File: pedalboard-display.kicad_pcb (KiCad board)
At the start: 2 copper layers, 174 x 111 mm, 206 parts, among them J1 LED-IN, J2 LED-OUT, J3 OLED

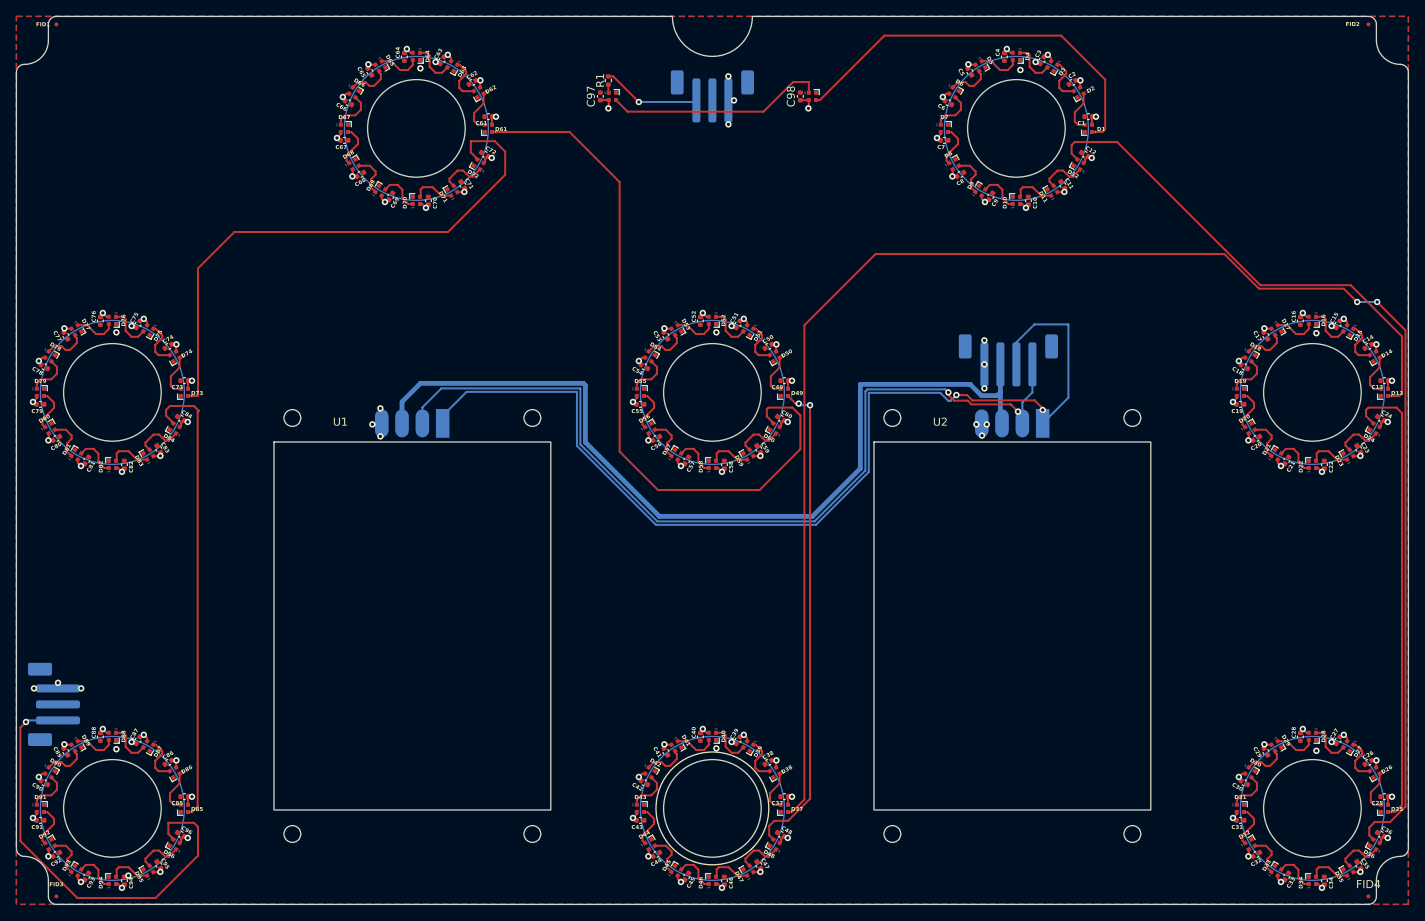
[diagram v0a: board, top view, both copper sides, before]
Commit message: Fix Silkscreen warnings
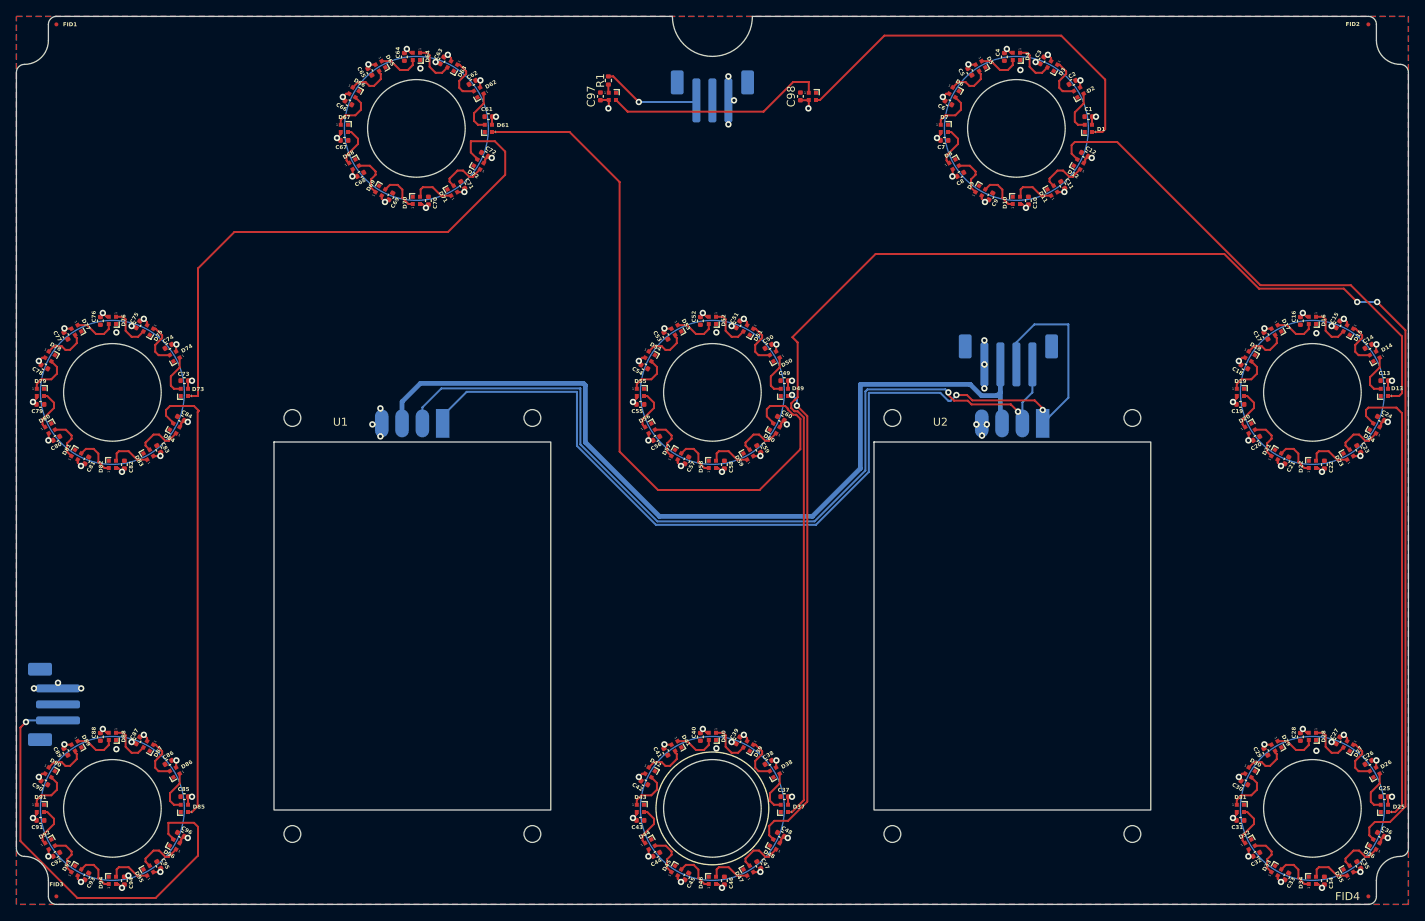
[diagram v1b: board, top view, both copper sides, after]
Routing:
- net /Led Ring B/D_IN: track 211.6 -> 213.7 mm
- net /Led Ring B/D_OUT: track 60.9 -> 60.1 mm

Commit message: Cleanup tracks (move vias to save space
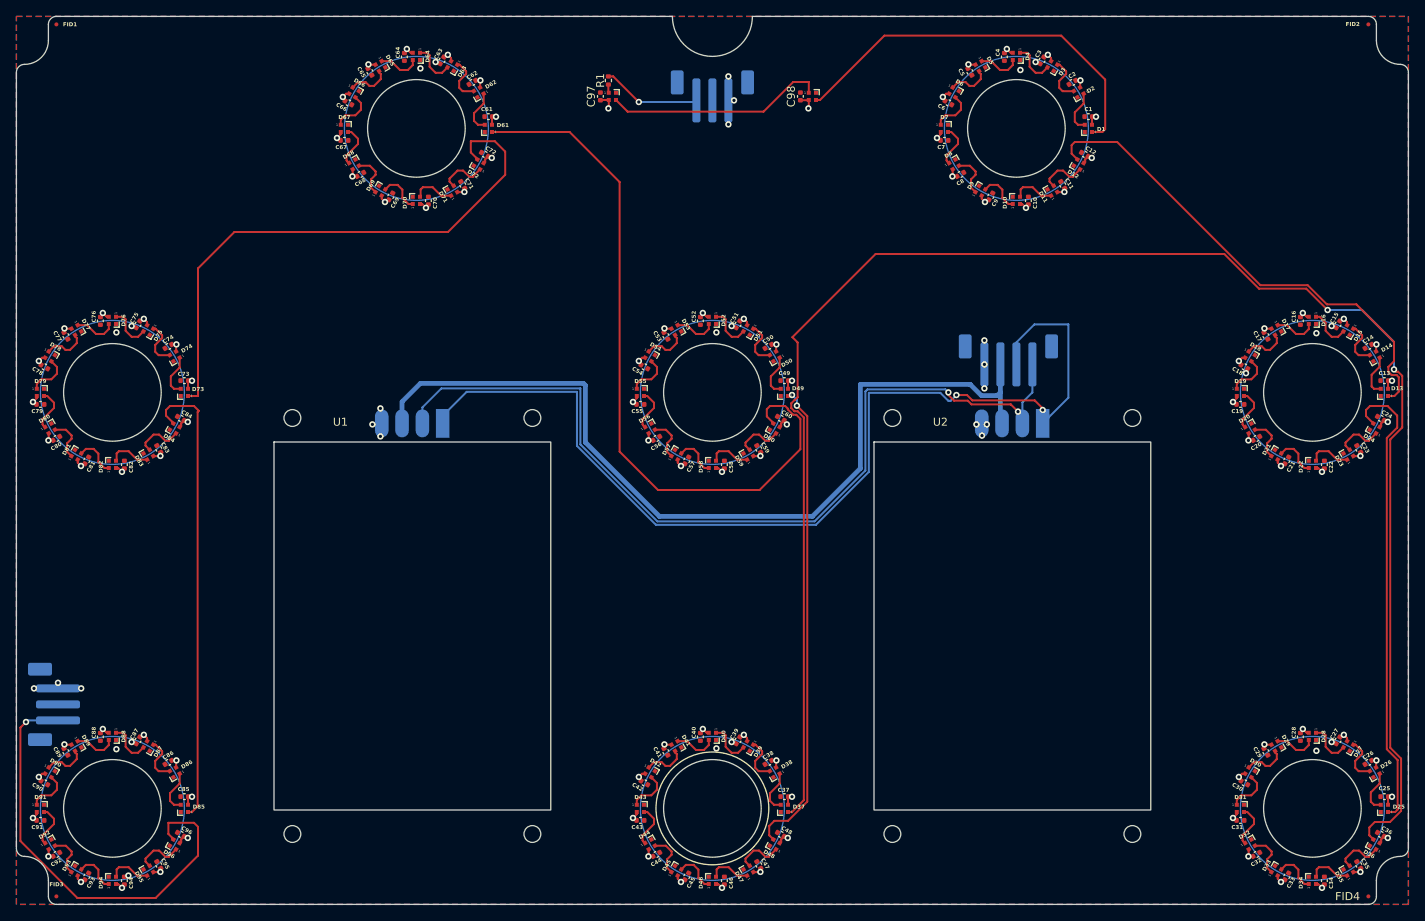
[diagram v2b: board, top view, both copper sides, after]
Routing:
- net GND: track 26.7 -> 25.2 mm, vias 32 -> 33
- net /I2C_SDA: track 127.8 -> 126.9 mm
- net /Led Ring B/D_IN: track 213.7 -> 212.9 mm
- net /Led Ring F/D_IN: track 62.6 -> 61.9 mm

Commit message: Cleanup tracks
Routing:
- net /I2C_SDA: track 126.9 -> 124.9 mm
- net +3.3V: track 110.4 -> 108.8 mm

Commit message: Cleanup vias
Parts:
- moved R1 0.77 mm to (93.4, 33.5), turned to 0 degrees
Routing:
- net GND: track 25.2 -> 20.4 mm
- net Net-(J1-Pin_3): track 12.1 -> 13.4 mm
- net VCC: track 98.9 -> 97.8 mm
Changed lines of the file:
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@@
 	(footprint "Resistor_SMD:R_0402_1005Metric"
 		(layer "F.Cu")
-		(at 94 33.01 -90)
+		(at 93.4 33.5)
 		(descr "Resistor SMD 0402 (1005 Metric), square (rectangular) end terminal, IPC_7351 nominal, (Body size source: IPC-SM-782 page 72, https://www.pcb-3d.com/wordpress/wp-content/uploads/ipc-sm-782a_amendment_1_and_2.pdf), generated with kicad-footprint-generator")
 		(tags "resistor")
 		(property "Reference" "R1"
-			(at 0 1 90)
+			(at 0 1 360)
 			(layer "F.SilkS")
 			(effects
@@
 		)
 		(property "Value" "330"
-			(at 0 1.17 90)
+			(at 0 1.17 360)
 			(layer "F.Fab")
 			(effects
@@
 		)
 		(property "Footprint" "Resistor_SMD:R_0402_1005Metric"
-			(at 0 0 90)
+			(at 0 0 360)
 			(layer "F.Fab")
 			(hide yes)
@@
 		)
 		(property "Datasheet" "https://www.passivecomponent.com/wp-content/uploads/chipR/ASC_WR.pdf"
-			(at 0 0 90)
+			(at 0 0 360)
 			(layer "F.Fab")
 			(hide yes)
@@
 		)
 		(property "Description" ""
-			(at 0 0 90)
+			(at 0 0 360)
 			(layer "F.Fab")
 			(hide yes)
@@
 		)
 		(property "Supplier" "https://www.digikey.ch/en/products/detail/walsin-technology-corporation/WR04X3300FTL/13239224"
-			(at 189 67 90)
+			(at 189 67 360)
 			(layer "F.Fab")
 			(hide yes)
@@
 		(attr smd)
 		(fp_line
-			(start -0.153641 0.38)
-			(end 0.153641 0.38)
+			(start -0.153641 -0.38)
+			(end 0.153641 -0.38)
 			(stroke
 				(width 0.12)
@@
 		)
 		(fp_line
-			(start -0.153641 -0.38)
-			(end 0.153641 -0.38)
+			(start -0.153641 0.38)
+			(end 0.153641 0.38)
 			(stroke
 				(width 0.12)
@@
 		)
 		(fp_line
-			(start -0.93 0.47)
-			(end -0.93 -0.47)
+			(start -0.93 -0.47)
+			(end 0.93 -0.47)
 			(stroke
 				(width 0.05)
@@
 		)
 		(fp_line
-			(start 0.93 0.47)
-			(end -0.93 0.47)
+			(start -0.93 0.47)
+			(end -0.93 -0.47)
 			(stroke
 				(width 0.05)
@@
 		)
 		(fp_line
-			(start -0.93 -0.47)
-			(end 0.93 -0.47)
+			(start 0.93 -0.47)
+			(end 0.93 0.47)
 			(stroke
 				(width 0.05)
@@
 		)
 		(fp_line
-			(start 0.93 -0.47)
-			(end 0.93 0.47)
+			(start 0.93 0.47)
+			(end -0.93 0.47)
 			(stroke
 				(width 0.05)
@@
 		)
 		(fp_line
-			(start -0.525 0.27)
-			(end -0.525 -0.27)
+			(start -0.525 -0.27)
+			(end 0.525 -0.27)
 			(stroke
 				(width 0.1)
@@
 		)
 		(fp_line
-			(start 0.525 0.27)
-			(end -0.525 0.27)
+			(start -0.525 0.27)
+			(end -0.525 -0.27)
 			(stroke
 				(width 0.1)
@@
 		)
 		(fp_line
-			(start -0.525 -0.27)
-			(end 0.525 -0.27)
+			(start 0.525 -0.27)
+			(end 0.525 0.27)
 			(stroke
 				(width 0.1)
@@
 		)
 		(fp_line
-			(start 0.525 -0.27)
-			(end 0.525 0.27)
+			(start 0.525 0.27)
+			(end -0.525 0.27)
 			(stroke
 				(width 0.1)
@@
 		)
 		(fp_text user "${REFERENCE}"
-			(at 0 0 90)
+			(at 0 0 360)
 			(layer "F.Fab")
 			(effects
@@
 		)
 		(pad "1" smd roundrect
-			(at -0.51 0 270)
+			(at -0.51 0)
 			(size 0.54 0.64)
 			(layers "F.Cu" "F.Paste" "F.Mask")
@@
 		)
 		(pad "2" smd roundrect
-			(at 0.51 0 270)
+			(at 0.51 0)
 			(size 0.54 0.64)
 			(layers "F.Cu" "F.Paste" "F.Mask")
@@
 	)
 	(segment
-		(start 94.05 36.45)
-		(end 94 36.5)
-		(width 0.25)
-		(layer "F.Cu")
-		(net 7)
-	)
-	(segment
 		(start 172.803848 120.071797)
 		(end 173.210934 119.664711)
@@
 	)
 	(segment
-		(start 94.05 35.45)
-		(end 94.05 36.45)
-		(width 0.25)
-		(layer "F.Cu")
-		(net 7)
-	)
-	(segment
 		(start 176.04106 116.04106)
 		(end 176 116)
@@
 	)
 	(via
-		(at 94 36.5)
+		(at 94.1 36)
 		(size 0.8)
 		(drill 0.4)
@@
 	)
 	(via
-		(at 65.5 77.5)
+		(at 65.6 77.3)
 		(size 0.8)
 		(drill 0.4)
@@
 	)
 	(via
-		(at 109.7 35.5)
+		(at 109 35.5)
 		(size 0.8)
 		(drill 0.4)
@@
 	)
 	(via
-		(at 25.2 108.3)
+		(at 25.2 109)
 		(size 0.8)
 		(drill 0.4)
@@
 	)
 	(via
-		(at 65.5 74)
+		(at 66.3 76)
 		(size 0.8)
 		(drill 0.4)
@@
 	)
 	(via
-		(at 64.5 76)
+		(at 65 76)
 		(size 0.8)
 		(drill 0.4)
@@
 	)
 	(segment
-		(start 65.668 74.168)
-		(end 65.5 74)
-		(width 0.25)
-		(layer "B.Cu")
-		(net 8)
-	)
-	(segment
 		(start 25.2 109)
 		(end 28.1 109)
@@
 	)
 	(segment
-		(start 65.668 75.8728)
-		(end 65.668 74.168)
-		(width 0.25)
-		(layer "B.Cu")
-		(net 8)
-	)
-	(segment
 		(start 141 68.5)
 		(end 141 65.5)
@@
 	)
 	(segment
-		(start 65.668 77.332)
-		(end 65.5 77.5)
-		(width 0.25)
-		(layer "B.Cu")
-		(net 8)
-	)
-	(segment
-		(start 64.6272 75.8728)
-		(end 64.5 76)
-		(width 0.25)
-		(layer "B.Cu")
-		(net 8)
-	)
-	(segment
 		(start 25.2 109)
 		(end 22.2 109)
@@
 	)
 	(segment
-		(start 25.2 109)
-		(end 25.2 108.3)
-		(width 0.25)
-		(layer "B.Cu")
-		(net 8)
-	)
-	(segment
 		(start 141 68.5)
 		(end 141 71.5)
@@
 	)
 	(segment
-		(start 65.668 75.8728)
-		(end 64.6272 75.8728)
-		(width 0.25)
-		(layer "B.Cu")
-		(net 8)
-	)
-	(segment
-		(start 109 35.5)
-		(end 109.7 35.5)
-		(width 0.25)
-		(layer "B.Cu")
-		(net 8)
-	)
-	(segment
 		(start 109 35.5)
 		(end 109 32.5)
@@
 	)
 	(segment
-		(start 94.6 32.5)
-		(end 94 32.5)
+		(start 93.59 32.8)
+		(end 92.89 33.5)
+		(width 0.25)
+		(layer "F.Cu")
+		(net 14)
+	)
+	(segment
+		(start 94.750617 33.197803)
+		(end 94.352814 32.8)
 		(width 0.25)
 		(layer "F.Cu")
@@
 	)
 	(segment
-		(start 94.6 32.5)
-		(end 97.8 35.7)
+		(start 94.352814 32.8)
+		(end 93.59 32.8)
 		(width 0.25)
 		(layer "F.Cu")
@@
 	)
 	(via
-		(at 97.8 35.7)
+		(at 94.750617 33.197803)
 		(size 0.8)
 		(drill 0.4)
@@
 	)
 	(segment
-		(start 97.8 35.7)
+		(start 97.252814 35.7)
 		(end 104.8 35.7)
 		(width 0.25)
 		(layer "B.Cu")
+		(net 14)
+	)
+	(segment
+		(start 94.750617 33.197803)
+		(end 97.252814 35.7)
+		(width 0.25)
+		(layer "B.Cu")
